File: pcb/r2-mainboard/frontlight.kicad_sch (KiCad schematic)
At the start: 0 parts

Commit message: R2: WP6a -- frontlight drawn, and it closes a hole rather than adding a feature
The netlist said it plainly before this sheet existed:

    +5V2_FL    C147.1  J6.44  J6.7      <- three loads, no source
    +VSYS_FL   R72.1   U22.1            <- a shunt into an ammeter, going nowhere

R1 fed +5V2_FL from +5V_DCDC through shunt R72, so the panel saw about 4.99 V.
WP2 moved the frontlight to the cell -- power_mon's U22 ch3 became
+VSYS -> +VSYS_FL -- and left the converter to WP6. Until now the rail was
orphaned at one end and the shunt dead-ended at the other. Verified against R1
by exporting its netlist from a copy in /tmp; pcb/mainboard/ never touched.

U53 is a second TPS61022, same topology as U12 and deliberately the same
feedback values: 732k/100k = 4.992 V. That adds no new passive line items, and
one DFE322512F now covers L10, L12, L13 and L33.

Why ~5.0 V and not 5.2: the net name was already wrong in R1, where it came off
a 5.0 V rail. epd-port.md 7 left "confirm or rename" to WP6. Confirmed at R1's
proven value and the name kept -- the panel-side circuit is unknown because the
panel is, so matching what R1 actually delivered is the conservative choice, and
renaming would touch frozen epd.kicad_sch for a cosmetic gain. If a chosen panel
wants a different string voltage it is two resistors.

The architecture is R1's and is not obvious, so it is written down: there is no
LED driver on this board and there was none on R1. The board supplies a voltage
rail plus FL_EN/FL_PWM1/FL_PWM2 to J6, and the panel's tail regulates the LED
current and does the dimming. FL_EN now has four nodes -- MCU, J6, U53.EN and
its pull-down -- because one signal means "frontlight on" and there is no case
where the boost and the panel side should disagree.

Sized deliberately oversized: a 3 A part for ~100 mA. The alternative is a new
IC, footprint, inductor and stock check to save a few hundred uA on a rail that
is off whenever the light is off. TPS61022 draws 27 uA + 0.9 uA running, 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
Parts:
- added C514, C515: 22uF/10V, Capacitor_SMD:C_0805_2012Metric, symbol Device:C
- added C516: 100nF/16V, Capacitor_SMD:C_0402_1005Metric, symbol Device:C
- added L33: 1uH 4.8A Isat, Inductor_SMD:L_1210_3225Metric, symbol Device:L
- added R505: 732k, Resistor_SMD:R_0402_1005Metric, symbol Device:R
- added R506, R507: 100k, Resistor_SMD:R_0402_1005Metric, symbol Device:R
- added U53: TPS61022RWUR, Package_DFN_QFN:Texas_RWU0007A_VQFN-7_2x2mm_P0.5mm, symbol Converter_DCDC:TPS61022
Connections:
- new net: L33.2, U53.2 (SW)
- new net: R505.2, R506.1, U53.4 (FB)
- new net +5V2_FL: C515.1, R505.1, U53.3 (VOUT)
- new net +VSYS_FL: C514.1, C516.1, L33.1, U53.7 (VIN)
- new net GND: C514.2, C515.2, C516.2, R506.2, R507.1, R507.2, U53.1 (GND), U53.5 (EN), U53.6 (MODE)
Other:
- note added: "*** LED current and does the dimming."
- note added: "*** No LED driver on this board, and none on R1. The board supplies this"
- note added: "*** rail plus FL_EN/FL_PWM1/FL_PWM2 to J6; the panel tail regulates the"
- note added: "FL_EN starts the boost and also reaches J6.43 -- one signal, one intent."
- note added: "R1 delivered, from +5V_DCDC through shunt R72. The name +5V2_FL was"
- note added: "U12 on power.kicad_sch: 0.600 x (1 + 732k/100k) = 4.992 V. That is what"
- note added: "U53 is a second TPS61022, same topology and the same feedback values as"
- note added: "already wrong in R1 and is kept: it names the rail, not its voltage."
- note added: "frontlight -- the panel LED anode rail. See docs/frontlight.md."

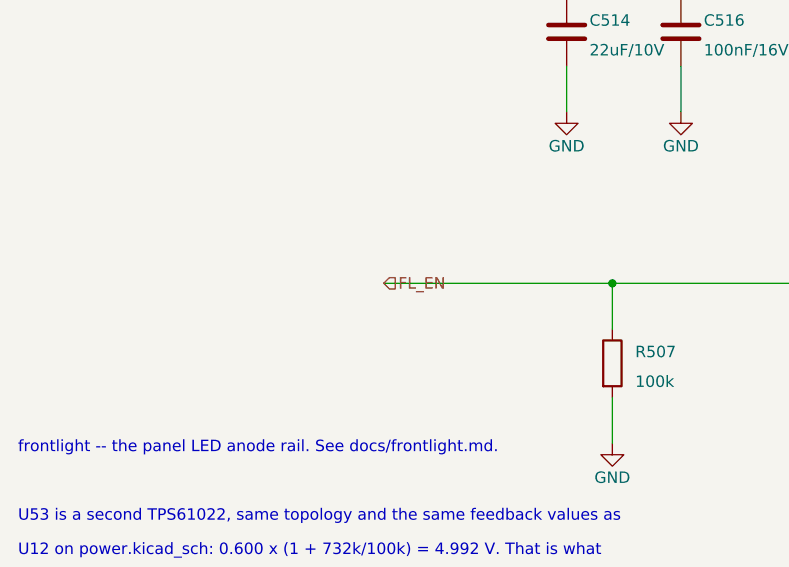
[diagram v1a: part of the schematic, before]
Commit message: R2: WP6b -- io_expansion drawn; Stage C capture is complete
Two FPC connectors, two gated rails, seven MCU pins, everything DNP.
NOTES-R2-plan.md constraint 3 wants touch and pen "addable without a respin";
this sheet is that provision, and it is honest about which half of the promise
is certain:

  certain  -- the seven MCU pins exist and are routed, and +3V3_TOUCH /
              +3V3_PEN exist. Those are what would otherwise force a
              whole-board respin.
  a guess  -- the FPC pad order, because neither the touch controller nor the
              digitizer is chosen and the panel is not either.

docs/io-expansion.md 5 puts that in front of the owner as the last open
decision in Stage C, with three ways to close it, rather than burying it.

PC4/PC5 are USART3_TX/RX at AF0 -- verified in stm32g0b1.pdf's
alternate-function table, both free, and the one allocation here that is not
interchangeable. The other five are ordinary GPIO. Touch adds no I2C pins: it
joins the existing always-on bus, and SCL_AON/SDA_AON now carry J22.3/J22.4
alongside the charger, gauge and three INA3221s. Two spares remain, and which
two was deliberate -- PA12 (USB-DP capable) and PB12 (ADC-capable) are the two
with a capability the rest lack.

Everything DNP is coherent, not lazy: with no connector fitted there is no
load, so a fitted load switch would be two parts powering nothing. It also
means these two TPS22914s consume none of the thin LCSC stock epd-port.md 7
flags, so that stays a two-part problem.

A FOURTH SILENT SHORT, and this time the tooling caught it before the netlist
did. The connectors' GND pins dropped from their own label column and ran
straight through the two anchors below -- putting SCL_AON, SDA_AON, PEN_TXD
and PEN_RXD on GND. The entire always-on I2C bus was shorted to ground and ERC
said nothing.

So schgen.Sheet.check_label_crossings() now runs inside render() for every
generator: no wire may pass *through* a label anchor it does not end at. Ending
at an a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
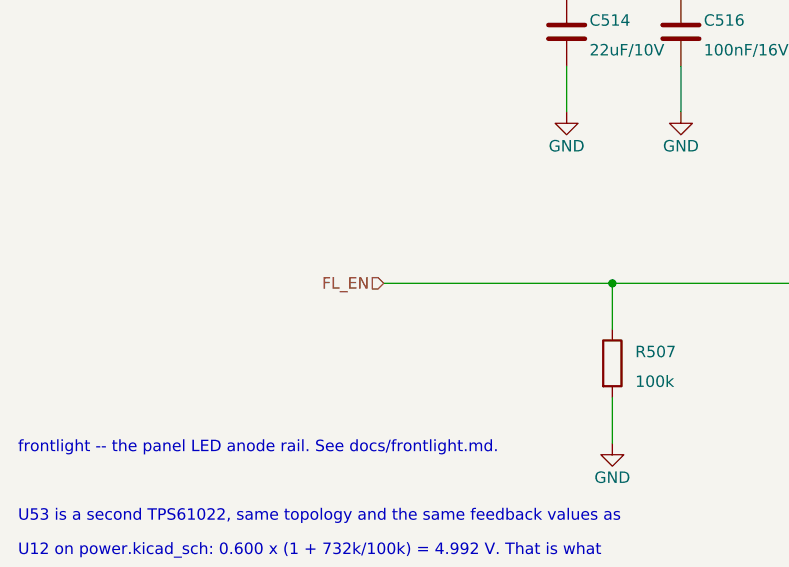
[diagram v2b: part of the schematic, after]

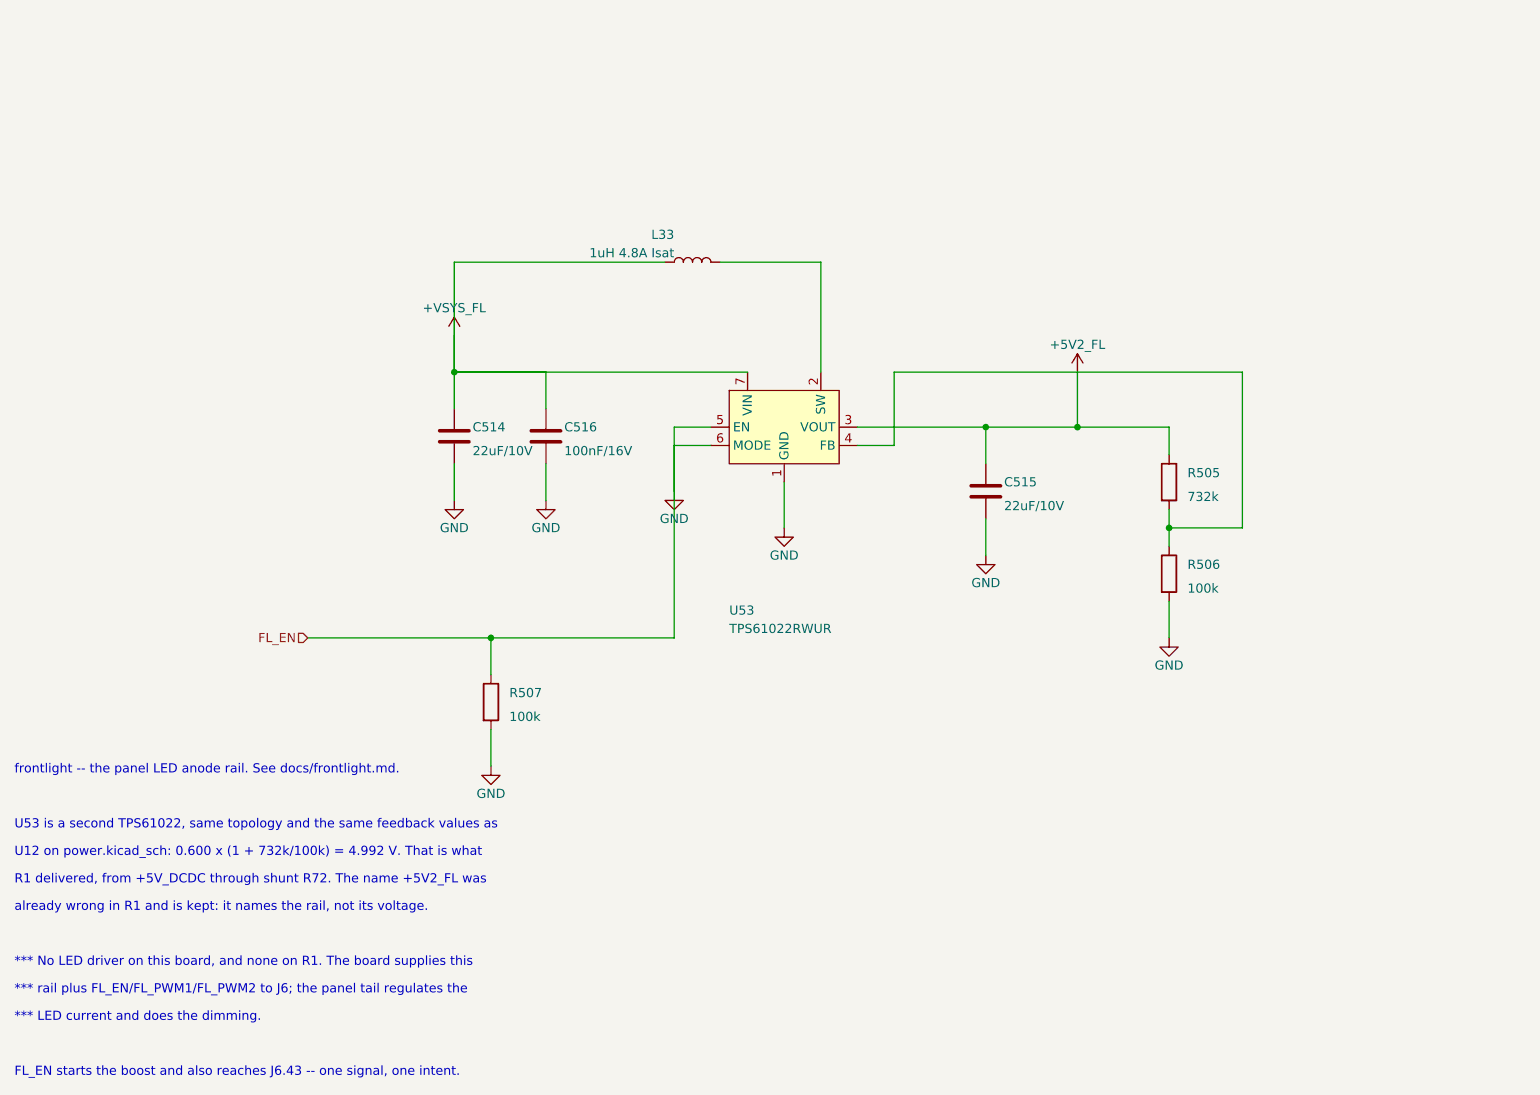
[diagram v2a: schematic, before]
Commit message: R2: WP6 -- frontlight captured; it is a current driver now, not a rail
Implements docs/frontlight.md. The old sheet boosted +VSYS_FL to a 4.99 V rail
and let the panel regulate its own LED current, which is what R1 did -- R1 drove
an adapter board. GDEP103TC2-FT11's frontlight is bonded and its tail is
LED1+/LED1-/LED2+/LED2-: bare anodes and cathodes. So U53's TPS61022, its
feedback divider and the +5V2_FL net are gone, replaced by an LM3630A driving
two independently dimmed strings from +VSYS_FL, plus J24 for the tail.

Safe to regenerate rather than patch: the committed sheet's line multiset was
identical to a fresh generator run, differing only in element order, so it had
never been saved in Eeschema.

Three geometry decisions are load-bearing, not cosmetic. The symbol's pin order
was chosen twice over: SW sits beside IN because a boost wants IN -> L -> SW
adjacent, and HWEN is the lowest left pin so its 100k pull-down drops into empty
space instead of across SCL/SDA. Crossing wires are not connected in KiCad, so
that arrangement is legal and invisible -- it is the shape of the four silent
shorts of 2026-08-16, one of which shorted this same I2C bus to GND. SEL rises
to the rail in its own column for the same reason.

R509 straps SEL to IN. Grounded, the LM3630A answers at 7-bit 0x36, which is
where max17048.pdf fixes the fuel gauge; two devices on one address would take
down the always-on bus and the charger with it.

Verified: check_grid and check_label_crossings pass (they run at render time);
netlist joins FL_EN across four nodes, FL_PWM1/SCL_AON/SDA_AON across sheets,
+VSYS_FL to U53.IN, and the LED anode to C515/OVP/J24.1/J24.5; check_ucf 0
failures; ERC adds no new category. Rendered to PNG and read four times -- the
first three had text collisions that only looking would have caught, including
D34's reference printing mirrored.

schgen gains an optional prop_angle so a part placed at 180 can keep its text
upright; the default is unchanged. wire_root gain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
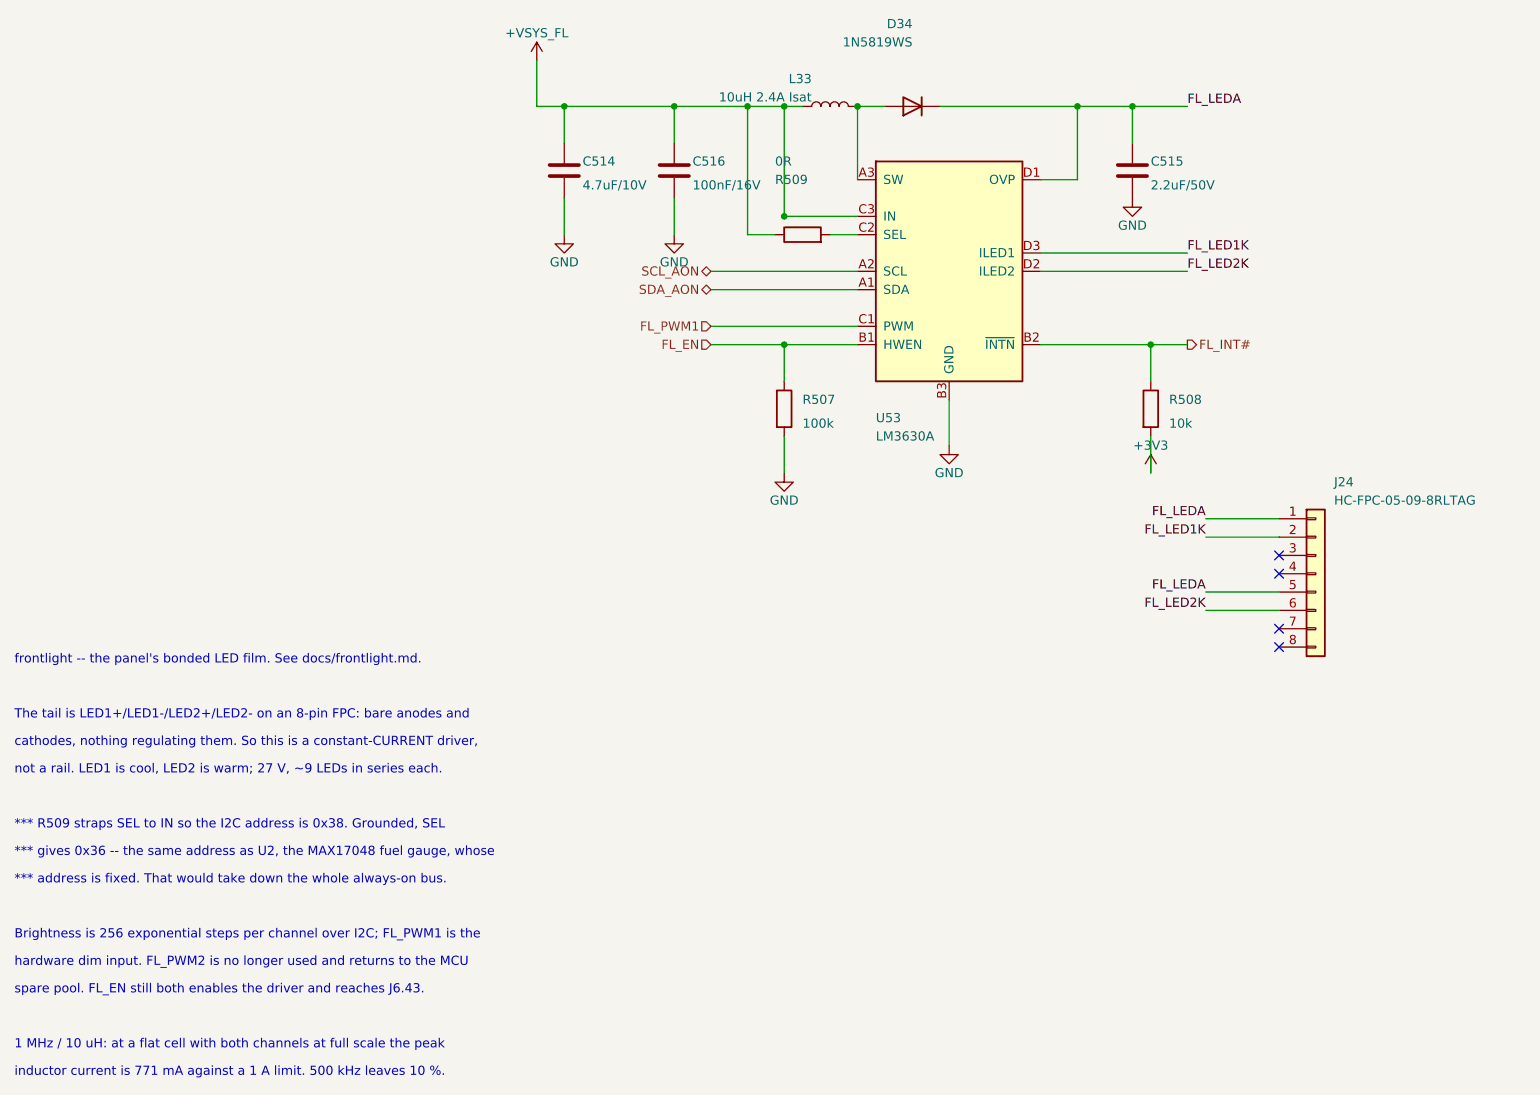
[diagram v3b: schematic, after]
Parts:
- removed R505: 732k, Resistor_SMD:R_0402_1005Metric, symbol Device:R
- removed R506: 100k, Resistor_SMD:R_0402_1005Metric, symbol Device:R
- removed U53: TPS61022RWUR, Package_DFN_QFN:Texas_RWU0007A_VQFN-7_2x2mm_P0.5mm, symbol Converter_DCDC:TPS61022
- added D34: 1N5819WS, footprints:D_SOD-323_Alt, symbol Device:D
- added J24: HC-FPC-05-09-8RLTAG, footprints:HC-FPC-05-09-8RLTAG, symbol Connector_Generic:Conn_01x08
- added R508: 10k, Resistor_SMD:R_0402_1005Metric, symbol Device:R
- added R509: 0R, Resistor_SMD:R_0402_1005Metric, symbol Device:R
- added U53: LM3630A, r2:Texas_YFQ0012_DSBGA-12_1.91x1.39mm_Layout3x4_P0.4mm, symbol r2:LM3630A
- C514: value 22uF/10V -> 4.7uF/10V; footprint Capacitor_SMD:C_0805_2012Metric -> Capacitor_SMD:C_0603_1608Metric
- C515: value 22uF/10V -> 2.2uF/50V
- L33: value 1uH 4.8A Isat -> 10uH 2.4A Isat; footprint Inductor_SMD:L_1210_3225Metric -> Inductor_SMD:L_Changjiang_FNR4030S; LCSC C3224227 -> C167879
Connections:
- net +VSYS_FL: now also R509.1, U53.C3 (IN)
- net GND: now also U53.B3 (GND); no longer R507.1
- net at L33.2: now also D34.2 (A), U53.A3 (SW)
- net +5V2_FL renamed FL_LEDA
- net FL_LEDA: now also D34.1 (K), J24.1 (Pin_1), J24.5 (Pin_5), U53.D1 (OVP)
- new net: R509.2, U53.C2 (SEL)
- new net +3V3: R508.2
- new net FL_EN: R507.1, U53.B1 (HWEN)
- new net FL_INT#: R508.1, U53.B2 (~{INTN})
- new net FL_LED1K: J24.2 (Pin_2), U53.D3 (ILED1)
- new net FL_LED2K: J24.6 (Pin_6), U53.D2 (ILED2)
- new net FL_PWM1: U53.C1 (PWM)
- new net SCL_AON: U53.A2 (SCL)
- new net SDA_AON: U53.A1 (SDA)
- no-connect marks 0 -> 4
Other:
- note added: "*** R509 straps SEL to IN so the I2C address is 0x38. Grounded, SEL"
- note added: "*** address is fixed. That would take down the whole always-on bus."
- note added: "*** gives 0x36 -- the same address as U2, the MAX17048 fuel gauge, whose"
- note added: "1 MHz / 10 uH: at a flat cell with both channels at full scale the peak"
- note added: "Brightness is 256 exponential steps per channel over I2C; FL_PWM1 is the"
- note added: "The tail is LED1+/LED1-/LED2+/LED2- on an 8-pin FPC: bare anodes and"
- note added: "cathodes, nothing regulating them. So this is a constant-CURRENT driver,"
- note added: "frontlight -- the panel's bonded LED film. See docs/frontlight.md."
- note added: "hardware dim input. FL_PWM2 is no longer used and returns to the MCU"
- note added: "inductor current is 771 mA against a 1 A limit. 500 kHz leaves 10 %."
- note added: "not a rail. LED1 is cool, LED2 is warm; 27 V, ~9 LEDs in series each."
- note added: "spare pool. FL_EN still both enables the driver and reaches J6.43."
- note removed: "*** LED current and does the dimming."
- note removed: "*** No LED driver on this board, and none on R1. The board supplies this"
- note removed: "*** rail plus FL_EN/FL_PWM1/FL_PWM2 to J6; the panel tail regulates the"
- note removed: "FL_EN starts the boost and also reaches J6.43 -- one signal, one intent."
- note removed: "R1 delivered, from +5V_DCDC through shunt R72. The name +5V2_FL was"
- note removed: "U12 on power.kicad_sch: 0.600 x (1 + 732k/100k) = 4.992 V. That is what"
- note removed: "U53 is a second TPS61022, same topology and the same feedback values as"
- note removed: "already wrong in R1 and is kept: it names the rail, not its voltage."
- note removed: "frontlight -- the panel LED anode rail. See docs/frontlight.md."

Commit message: R2: MPNs into the schematic -- and five caps carry the wrong part number
Sourcing data lived in docs/*.md, not in the schematic, so the BOM the
fab would read had 3 of 96 lines with an MPN. Resolved every LCSC code
already on the board against LCSC's own catalogue and wrote MPN +
Manufacturer back: 53 -> 60 lines, 218 components. Added LCSC codes for
L10-L13, U42 and J22/J23 from the per-sheet docs.

Verified before writing: 321 refs and 519 nets identical before and
after, no duplicated properties, pre-existing MPNs untouched.

Cross-checking each passive value against the part its LCSC code
actually names found five wrong ones, all of them the ADC sense-divider
filter caps on power_mon:

  C91                 1nF/50V  carries C131394  = 100 nF
  C163 C164 C168 C169 1nF/25V  carries C6119801 = 470 nF

Left unwritten rather than cementing the error. C1523 (0402B102K500NT,
1 nF 50 V X7R 0402, JLC Basic, 5.3 M stock) covers both positions.

Also held back: U41, whose C39313 is XC6SLX16-**2**FTG256C while
fpga.md specifies the -3 speed grade.

frontlight.md cites C1848394 as the FPC connector on J22/J23; that code
is TPS22914BYFPR. The 6-pin sibling of J24's C5213749 is C5213748.

Co-Authored-By: Claude Opus 5 <noreply@anthropic.com>
Claude-Session: https://claude.ai/code/session_01MnesETWABbVdbcVnCKfKVs
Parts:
- D34: MPN (none) -> B5819WS; Manufacturer (none) -> Slkor
- J24: MPN (none) -> HC-FPC-05-09-8RLTAG; Manufacturer (none) -> HCTL
- L33: MPN (none) -> FNR4030S100MT; Manufacturer (none) -> cjiang
- U53: MPN (none) -> LM3630ATMX; Manufacturer (none) -> TI
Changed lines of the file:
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@@
+			)
+		)
+		(property "Manufacturer" "cjiang" (at 0 0 0)
+			(effects
+				(font
+					(size 1.27 1.27)
+				)
+				(hide yes)
+			)
+		)
+		(property "MPN" "FNR4030S100MT" (at 0 0 0)
+			(effects
+				(font
+					(size 1.27 1.27)
+				)
+				(hide yes)
 			)
 		)
@@
 			)
 		)
+		(property "Manufacturer" "TI" (at 0 0 0)
+			(effects
+				(font
+					(size 1.27 1.27)
+				)
+				(hide yes)
+			)
+		)
+		(property "MPN" "LM3630ATMX" (at 0 0 0)
+			(effects
+				(font
+					(size 1.27 1.27)
+				)
+				(hide yes)
+			)
+		)
 		(pin "D3"
 		)
@@
 			)
 		)
+		(property "Manufacturer" "Slkor" (at 0 0 0)
+			(effects
+				(font
+					(size 1.27 1.27)
+				)
+				(hide yes)
+			)
+		)
+		(property "MPN" "B5819WS" (at 0 0 0)
+			(effects
+				(font
+					(size 1.27 1.27)
+				)
+				(hide yes)
+			)
+		)
 		(pin "1"
 		)
@@
 			)
 		)
+		(property "Manufacturer" "HCTL" (at 0 0 0)
+			(effects
+				(font
+					(size 1.27 1.27)
+				)
+				(hide yes)
+			)
+		)
+		(property "MPN" "HC-FPC-05-09-8RLTAG" (at 0 0 0)
+			(effects
+				(font
+					(size 1.27 1.27)
+				)
+				(hide yes)
+			)
+		)
